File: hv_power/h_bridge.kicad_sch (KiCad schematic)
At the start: 37 parts, among them J12 Conn_02x03_Odd_Even, J3 Conn_01x01_Male, J6 V-, J9 V+, M5 NMOS_KELVIN, M6 NMOS_KELVIN, U29 THS4531, U5 UCC23511DWY, U6 UCC23511DWY

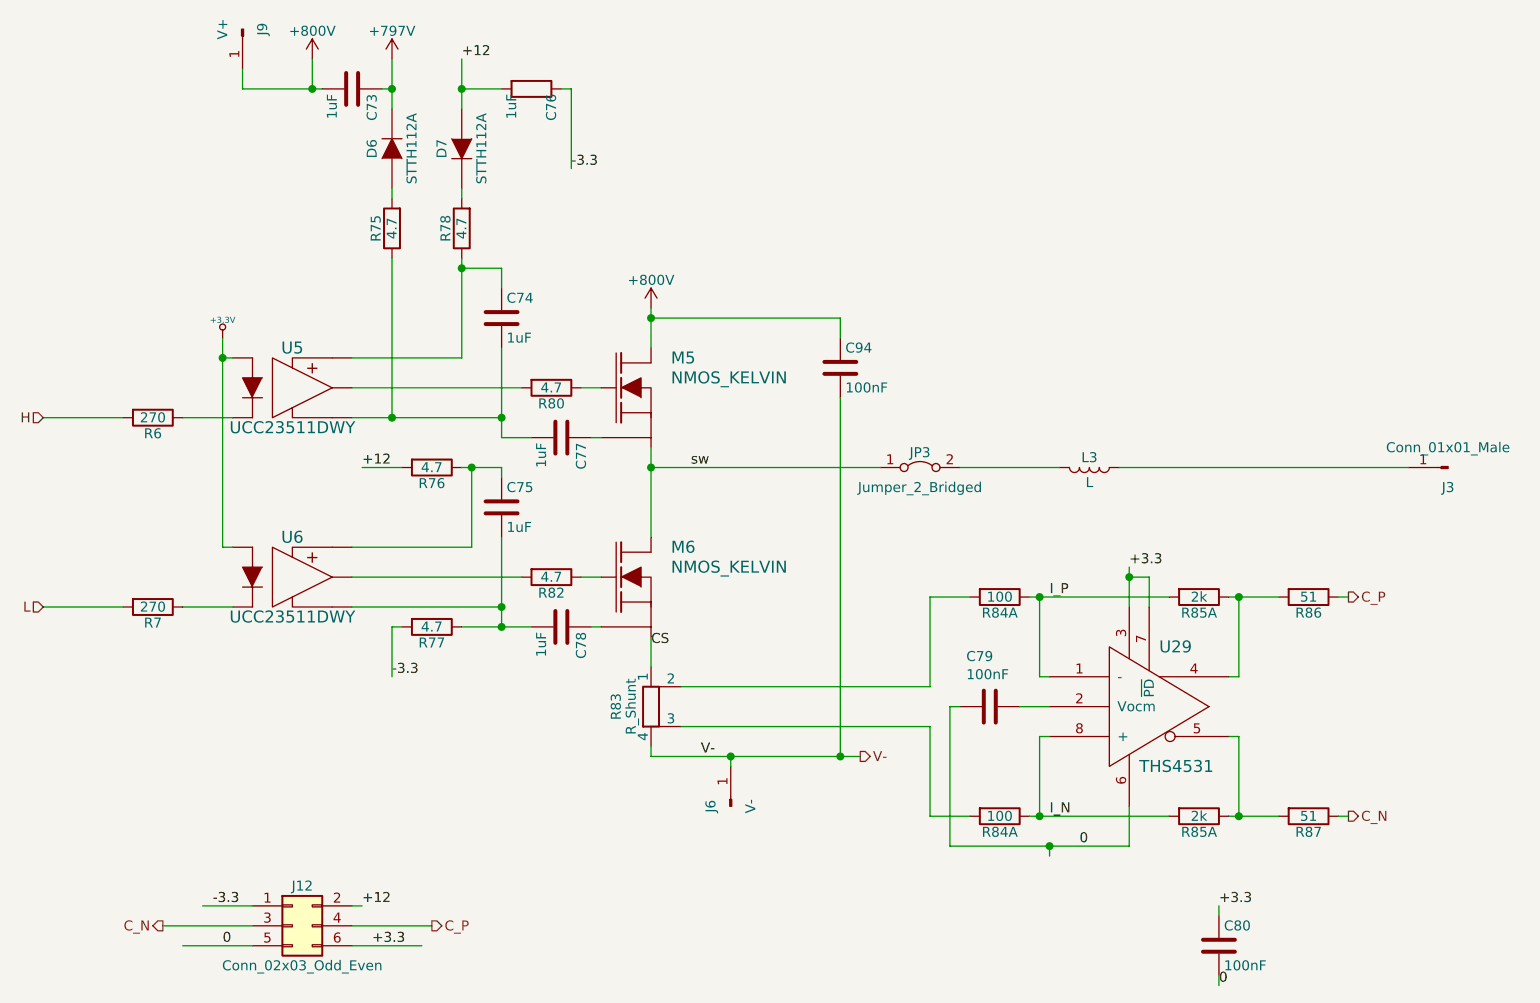
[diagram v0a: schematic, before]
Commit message: Moving to new CCU8 implementation. Moved trace and @arm scripts to octave archive.
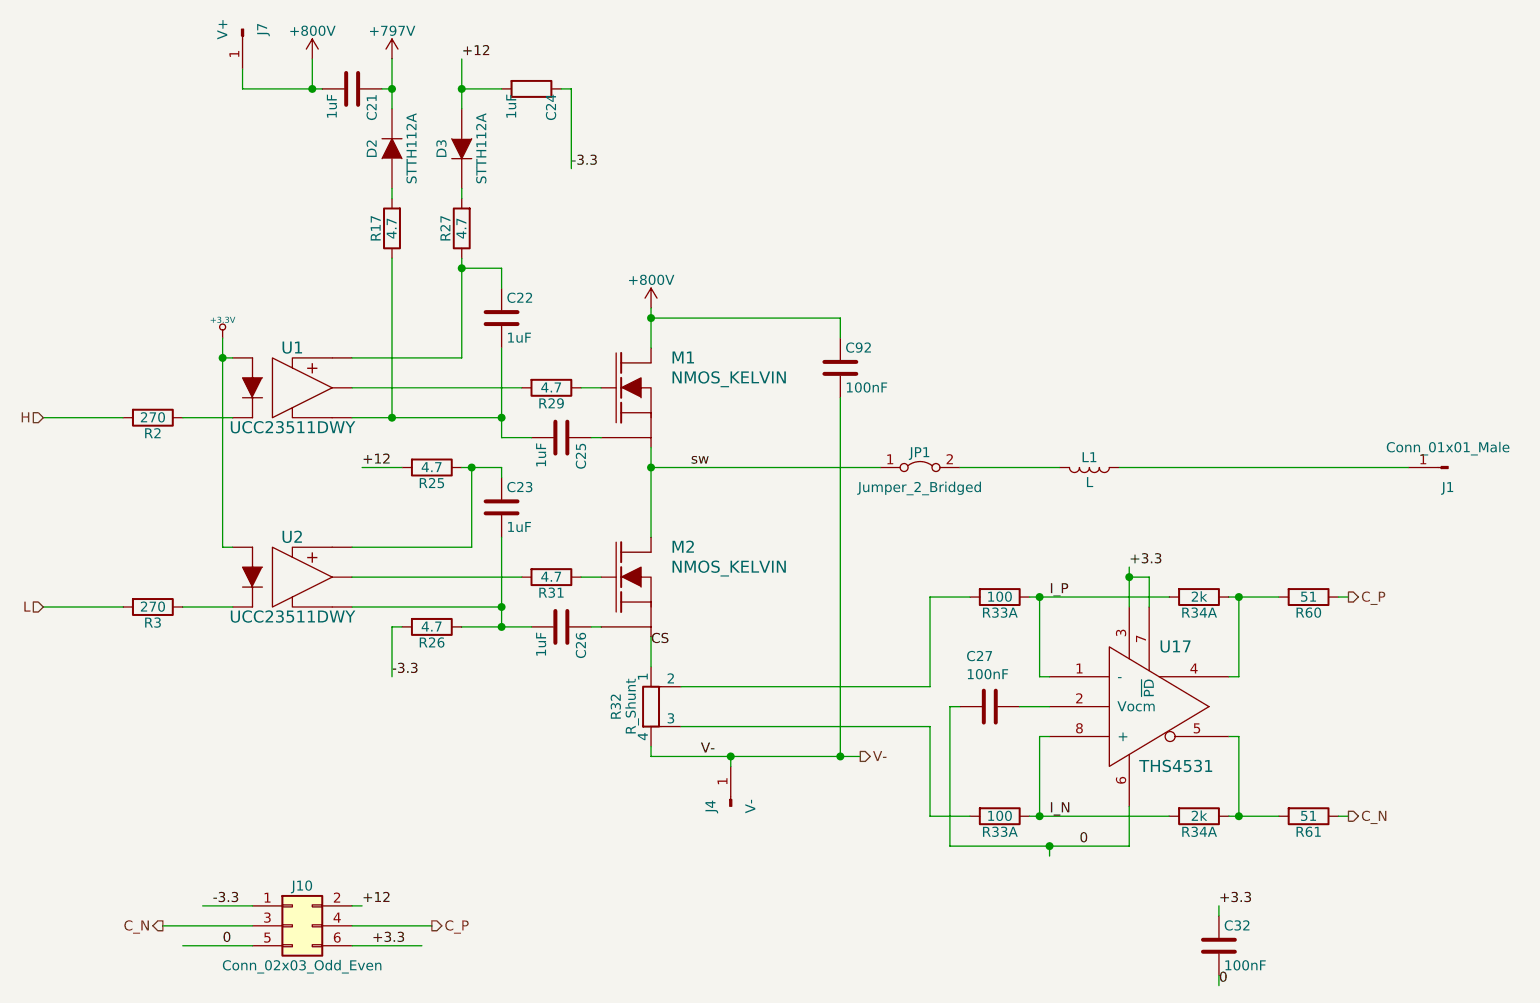
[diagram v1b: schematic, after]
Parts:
- J10: renamed from J12; Manufacturer Samtec -> (none)
- renumbered C73 to C21, C74 to C22, C75 to C23, C76 to C24, C77 to C25, C78 to C26, C79 to C27, C80 to C32, C94 to C92, D6 to D2, D7 to D3, J3 to J1, J6 to J4, J9 to J7, JP3 to JP1, L3 to L1, M5 to M1, M6 to M2, R75 to R17, R6 to R2, R76 to R25, R77 to R26, R78 to R27, R80 to R29, R7 to R3, R82 to R31, R83 to R32, R84 to R33, R85 to R34, R86 to R60, R87 to R61, U5 to U1, U29 to U17, U6 to U2

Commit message: Ordered new boards.
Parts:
- removed C21, C25, C26: 1uF, Capacitor_SMD:C_0805_2012Metric, symbol Device:C
- removed C27: 100nF, Capacitor_SMD:C_0603_1608Metric, symbol Device:C
- removed D2: STTH112A, 00_Passives:D_SMA, symbol Local:DIODE
- removed R17, R26: 4.7, Resistor_SMD:R_0603_1608Metric, symbol Device:R
- removed R60, R61: 51, Resistor_SMD:R_0603_1608Metric, symbol Device:R
- removed U17: THS4531, Package_SO:MSOP-8_3x3mm_P0.65mm, symbol Local:THS4531
- added C3: C, Capacitor_SMD:C_1206_3216Metric, symbol Device:C
- added R8: R, Resistor_SMD:R_1206_3216Metric, symbol Device:R
- added R9: 270, Resistor_SMD:R_2512_6332Metric, symbol Device:R
- added U7: TSV991ILT, Package_TO_SOT_SMD:SOT-23-5, symbol Amplifier_Operational:OPA333xxDBV
- C23, C32: footprint Capacitor_SMD:C_1206_3216Metric -> Capacitor_SMD:C_0805_2012Metric
- C24: symbol Device:R -> Device:C
- C92: footprint Capacitor_SMD:C_1812_4532Metric -> Capacitor_SMD:C_2220_5650Metric
- M1, M2: value NMOS_KELVIN -> TBD
- R27: footprint Resistor_SMD:R_0805_2012Metric -> Resistor_SMD:R_0603_1608Metric
- R31: footprint Resistor_SMD:R_0603_1608Metric -> Resistor_SMD:R_0805_2012Metric
- R33, R34: footprint Resistor_SMD:R_0603_1608Metric -> 00_Passives:ACASN
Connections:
- net +12: now also R27.1; no longer D3.A
- net +3.3: now also U7.5 (V+)
- net 0: now also C24.1, U7.2 (V-)
- net C_N: now also J10.4 (Pin_4), R34.1, U7.1; no longer J10.3 (Pin_3)
- net C_P: now also J10.3 (Pin_3), R34.2; no longer J10.4 (Pin_4)
- net I_N: now also R33.1, R34.4, U7.4 (-); no longer R33.1, R34.4
- net I_P: now also R33.2, R34.3, U7.3 (+); no longer R33.1, R34.4
- net V-: now also R8.2
- net sw: now also C3.1
- net at R32.3: now also R33.3; no longer R33.4
- net sw_g: now reaches M1.G, R29.1
- net sw_s: now reaches M1.KS (ks)
- net sw_s: now also C22.2, U1.4 (gnd)
- net sw_o: now reaches R29.2, U1.5 (out)
- net sw_+: now reaches C22.1, U1.6 (vcc)
- net sw_+: now also D3.C; no longer R27.1
- net at R27.2: now also D3.A; no longer D3.C
- net at M2.KS (ks): now also C23.2, U2.4 (gnd)
- net d1: now reaches R2.1, U1.3 (cathode)
- net d2: now reaches R3.1, U2.3 (cathode)
- net sw_m2: now reaches J1.1 (Pin_1), L1.1
- net sw_m2: now also R9.2
- net sw_m1: now reaches JP1.2 (B), L1.2
- net sw_m1: now also R9.1
- net -3.3 renamed V_servo
- net V_servo: no longer C24.1
- new net x: C3.2, R8.1
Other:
- moved on the sheet: D3, R27, R29, R33A, R33B, R34A, R34B

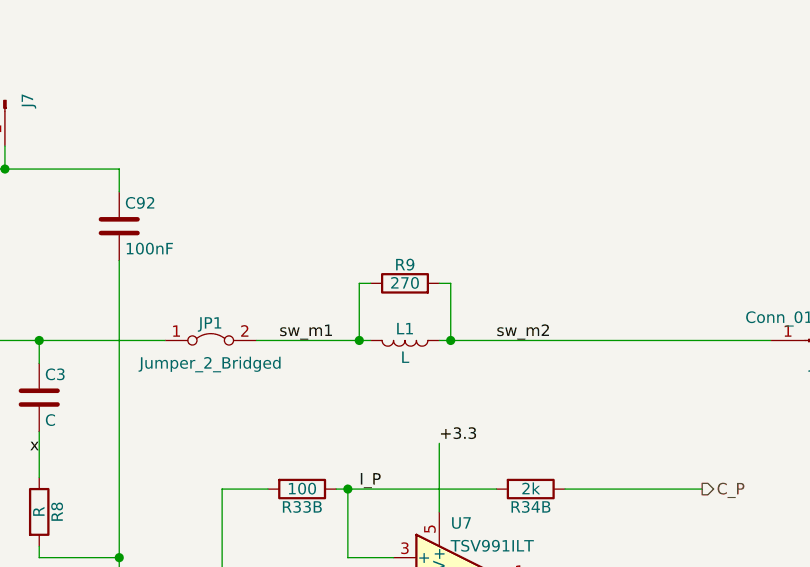
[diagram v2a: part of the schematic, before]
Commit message: Output snubber resistor put at 100 Ohm
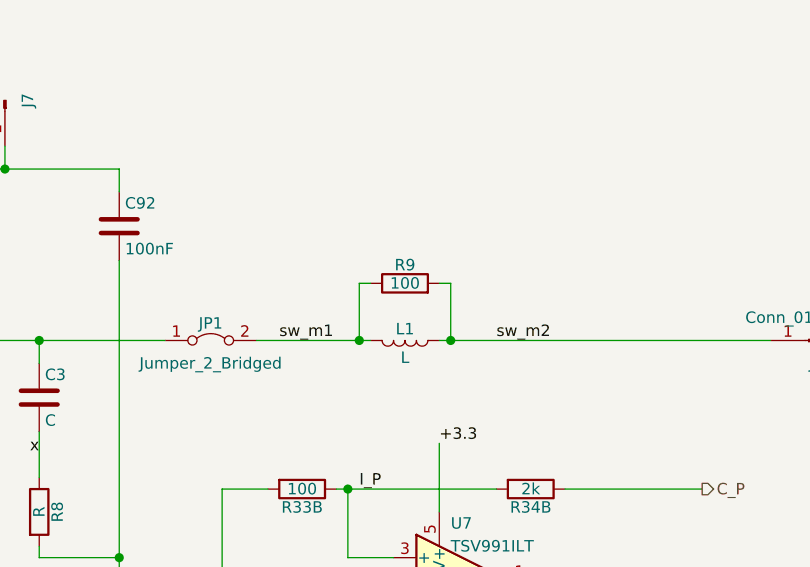
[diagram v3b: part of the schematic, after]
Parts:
- R9: value 270 -> 100
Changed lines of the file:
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@@
       (effects (font (size 1.27 1.27)))
     )
-    (property "Value" "270" (at 215.9 78.74 90)
+    (property "Value" "100" (at 215.9 78.74 90)
       (effects (font (size 1.27 1.27)))
     )

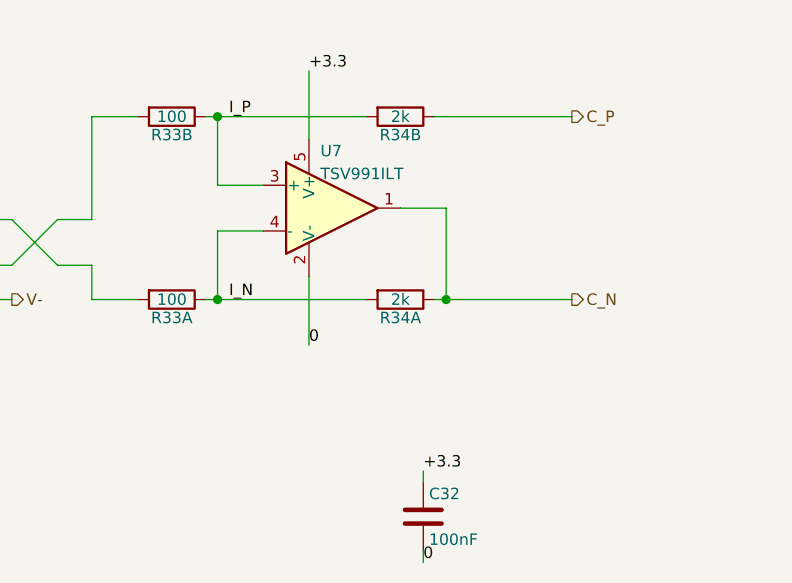
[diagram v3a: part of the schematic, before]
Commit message: Update current test to allow sending a profile.
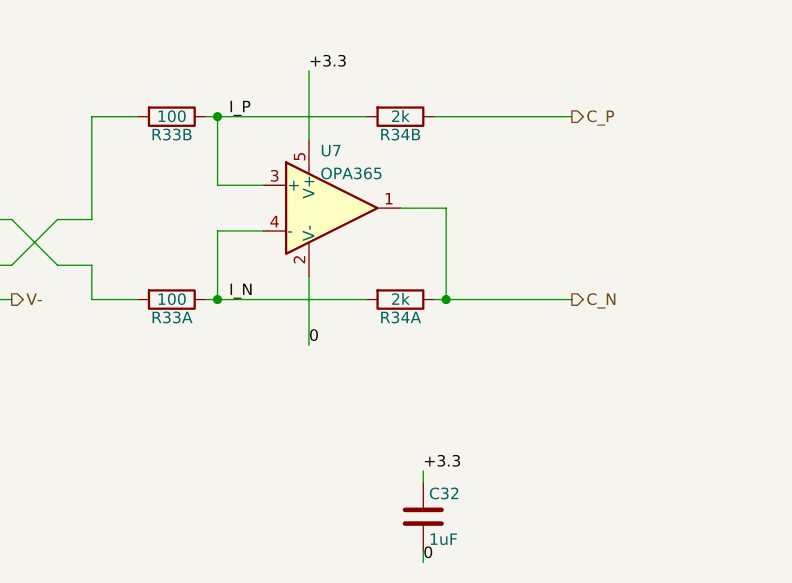
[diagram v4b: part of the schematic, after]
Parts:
- C32: value 100nF -> 1uF
- R9: PartNr (none) -> CRCW2512100RJNEGHP
- U7: value TSV991ILT -> OPA365
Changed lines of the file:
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@@
       (effects (font (size 1.27 1.27)) (justify left))
     )
-    (property "Value" "100nF" (at 233.045 148.59 0)
+    (property "Value" "1uF" (at 233.045 148.59 0)
       (effects (font (size 1.27 1.27)) (justify left))
     )
@@
       (effects (font (size 1.27 1.27)) hide)
     )
+    (property "PartNr" "CRCW2512100RJNEGHP" (at 215.9 78.74 90)
+      (effects (font (size 1.27 1.27)) hide)
+    )
     (pin "1")
     (pin "2")
@@
       (effects (font (size 1.27 1.27)) (justify left))
     )
-    (property "Value" "TSV991ILT" (at 220.98 107.95 0)
-      (effects (font (size 1.27 1.27)) (justify left))
-    )
+    (property "Value" "OPA365" (at 220.98 107.95 0)
+      (effects (font (size 1.27 1.27)) (justify left))
+    )
